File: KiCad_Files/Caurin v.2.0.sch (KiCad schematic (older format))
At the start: 23 parts, among them J1 ESQ-120-39-G-D, J2 Conn_01x12_Male, J3 Conn_01x09_Male, U1 STM32L476RGTx, Y1 32,768k

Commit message: Add shapes3D folder
Now all 3D models for the components are stored in a single folder, thanks to the Archive Plugin from https://github.com/MitjaNemec/Kicad_action_plugins.git
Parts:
- 16M1: symbol Device:Crystal_GND24 -> archive:Device_Crystal_GND24
- C1, C10, C2, C3, C4, C5, C6, C7, C8, C9: symbol Device:C_Small -> archive:Device_C_Small
- D1: symbol Device:LED -> archive:Device_LED
- J1: symbol SamacSys_Parts:ESQ-120-39-G-D -> archive:SamacSys_Parts_ESQ-120-39-G-D
- J2: symbol Connector:Conn_01x12_Male -> archive:Connector_Conn_01x12_Male
- J3: symbol Connector:Conn_01x09_Male -> archive:Connector_Conn_01x09_Male
- JP1: symbol Jumper:SolderJumper_3_Open -> archive:Jumper_SolderJumper_3_Open
- R1, R2, R3, R4: symbol Device:R_Small -> archive:Device_R_Small
- S1: symbol SamacSys_Parts:PTS636_SM43J_SMTR_LFS -> archive:SamacSys_Parts_PTS636_SM43J_SMTR_LFS
- U1: symbol MCU_ST_STM32L4:STM32L476RGTx -> archive:MCU_ST_STM32L4_STM32L476RGTx
- Y1: symbol Device:Crystal_Small -> archive:Device_Crystal_Small
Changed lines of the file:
@@
 	8550 5650 8600 5650
 $Comp
-L MCU_ST_STM32L4:STM32L476RGTx U1
+L archive:MCU_ST_STM32L4_STM32L476RGTx U1
 U 1 1 613E7615
 P 4625 5025
@@
 $EndComp
 $Comp
-L power:+3.3V #PWR0101
+L archive:power_+3.3V #PWR0101
 U 1 1 613F407B
 P 4675 3025
@@
 $EndComp
 $Comp
-L power:GND #PWR0102
+L archive:power_GND #PWR0102
 U 1 1 613FAFB6
 P 4625 6975
@@
 Connection ~ 4525 6925
 $Comp
-L Device:C_Small C2
+L archive:Device_C_Small C2
 U 1 1 614028ED
 P 4150 2050
@@
 $EndComp
 $Comp
-L Device:C_Small C7
+L archive:Device_C_Small C7
 U 1 1 6140503B
 P 4500 2050
@@
 $EndComp
 $Comp
-L Device:C_Small C8
+L archive:Device_C_Small C8
 U 1 1 614053AC
 P 4850 2050
@@
 $EndComp
 $Comp
-L Device:C_Small C9
+L archive:Device_C_Small C9
 U 1 1 6140585E
 P 5200 2050
@@
 $EndComp
 $Comp
-L Device:C_Small C1
+L archive:Device_C_Small C1
 U 1 1 61405AA7
 P 3800 2050
@@
 	4150 2250 4500 2250
 $Comp
-L power:+3.3V #PWR0103
+L archive:power_+3.3V #PWR0103
 U 1 1 61419BE2
 P 3800 1750
@@
 Connection ~ 3800 1850
 $Comp
-L power:GND #PWR0104
+L archive:power_GND #PWR0104
 U 1 1 6141BB41
 P 3800 2350
@@
 Connection ~ 3800 2250
 $Comp
-L Device:R_Small R2
+L archive:Device_R_Small R2
 U 1 1 6143BD59
 P 1900 3600
@@
 	2050 3600 2000 3600
 $Comp
-L Jumper:SolderJumper_3_Open JP1
+L archive:Jumper_SolderJumper_3_Open JP1
 U 1 1 61440C39
 P 1600 3600
@@
 	1750 3600 1800 3600
 $Comp
-L power:+3.3V #PWR0105
+L archive:power_+3.3V #PWR0105
 U 1 1 614479C3
 P 1600 3350
@@
 	1600 3350 1600 3400
 $Comp
-L power:GND #PWR0106
+L archive:power_GND #PWR0106
 U 1 1 61449D67
 P 1600 3850
@@
 	1600 3850 1600 3800
 $Comp
-L Device:Crystal_GND24 16M1
+L archive:Device_Crystal_GND24 16M1
 U 1 1 61450713
 P 1800 4950
@@
 $EndComp
 $Comp
-L power:GND #PWR0107
+L archive:power_GND #PWR0107
 U 1 1 61459354
 P 2725 5000
@@
 $EndComp
 $Comp
-L power:GND #PWR0108
+L archive:power_GND #PWR0108
 U 1 1 61459C79
 P 1325 5350
@@
 	2725 4950 2725 5000
 $Comp
-L Device:C_Small C3
+L archive:Device_C_Small C3
 U 1 1 6145E6A2
 P 1575 4700
@@
 	1800 4700 1800 4800
 $Comp
-L Device:C_Small C4
+L archive:Device_C_Small C4
 U 1 1 61463D13
 P 1575 5200
@@
 	3925 4725 3875 4725
 $Comp
-L power:GND #PWR0110
+L archive:power_GND #PWR0110
 U 1 1 614A349D
 P 1325 6650
@@
 	1325 6650 1325 6500
 $Comp
-L Device:C_Small C5
+L archive:Device_C_Small C5
 U 1 1 614A34A7
 P 1500 6125
@@
 	1400 6125 1325 6125
 $Comp
-L Device:C_Small C6
+L archive:Device_C_Small C6
 U 1 1 614A34B2
 P 1500 6500
@@
 	3925 6525 3875 6525
 $Comp
-L power:+3.3V #PWR0111
+L archive:power_+3.3V #PWR0111
 U 1 1 614C675D
 P 7350 2900
@@
 	7525 3125 7525 3075
 $Comp
-L power:GND #PWR0112
+L archive:power_GND #PWR0112
 U 1 1 614D5240
 P 7625 3125
@@
 	8425 3225 8425 3075
 $Comp
-L power:GND #PWR0113
+L archive:power_GND #PWR0113
 U 1 1 6158BF67
 P 1650 2600
@@
 $EndComp
 $Comp
-L Device:R_Small R1
+L archive:Device_R_Small R1
 U 1 1 6158C250
 P 1650 1750
@@
 $EndComp
 $Comp
-L power:+3.3V #PWR0114
+L archive:power_+3.3V #PWR0114
 U 1 1 6158C7F3
 P 1650 1550
@@
 	1650 1850 1650 1950
 $Comp
-L Device:C_Small C10
+L archive:Device_C_Small C10
 U 1 1 6159AFC7
 P 1850 2250
@@
 	3875 4925 3925 4925
 $Comp
-L Device:LED D1
+L archive:Device_LED D1
 U 1 1 61487691
 P 2700 2150
@@
 $EndComp
 $Comp
-L power:GND #PWR0109
+L archive:power_GND #PWR0109
 U 1 1 6149B9C4
 P 2700 2350
@@
 	2700 2300 2700 2350
 $Comp
-L Device:R_Small R4
+L archive:Device_R_Small R4
 U 1 1 614B0FAC
 P 2700 1850
@@
 	4675 3125 4725 3125
 $Comp
-L power:+3.3V #PWR0115
+L archive:power_+3.3V #PWR0115
 U 1 1 61613B7C
 P 7575 1250
@@
 GND
 $Comp
-L power:+5V #PWR0116
+L archive:power_+5V #PWR0116
 U 1 1 61683899
 P 6125 1850
@@
 $EndComp
 $Comp
-L power:+3.3V #PWR0117
+L archive:power_+3.3V #PWR0117
 U 1 1 61683C81
 P 6350 1850
@@
 $EndComp
 $Comp
-L power:GND #PWR0118
+L archive:power_GND #PWR0118
 U 1 1 61684B6A
 P 6250 2300
@@
 	8150 1450 8150 1275
 $Comp
-L power:+5V #PWR0119
+L archive:power_+5V #PWR0119
 U 1 1 61777ED3
 P 8775 1250
@@
 BUS_SCL1
 $Comp
-L Device:R_Small R3
+L archive:Device_R_Small R3
 U 1 1 614BCB98
 P 2050 5200
@@
 	7950 1450 7950 1275
 $Comp
-L power:GND #PWR0120
+L archive:power_GND #PWR0120
 U 1 1 6161F41F
 P 8050 1325
@@
 	1600 6500 1700 6500
 $Comp
-L Device:Crystal_Small Y1
+L archive:Device_Crystal_Small Y1
 U 1 1 614DD45F
 P 1700 6300
@@
 GND
 $Comp
-L SamacSys_Parts:ESQ-120-39-G-D J1
+L archive:SamacSys_Parts_ESQ-120-39-G-D J1
 U 1 1 613C51C6
 P 7650 6250
@@
 	10000 5950 10100 5950
 $Comp
-L SamacSys_Parts:PTS636_SM43J_SMTR_LFS S1
+L archive:SamacSys_Parts_PTS636_SM43J_SMTR_LFS S1
 U 1 1 6235C882
 P 1200 2250
@@
 Connection ~ 1650 2550
 $Comp
-L Connector:Conn_01x09_Male J3
+L archive:Connector_Conn_01x09_Male J3
 U 1 1 6251C245
 P 8250 1075
@@
 $EndComp
 $Comp
-L power:+BATT #PWR0152
+L archive:power_+BATT #PWR0152
 U 1 1 627D0227
 P 6625 1850
@@
 EXT_GPS_TX
 $Comp
-L Connector:Conn_01x12_Male J2
+L archive:Connector_Conn_01x12_Male J2
 U 1 1 6246EB1E
 P 8025 2875

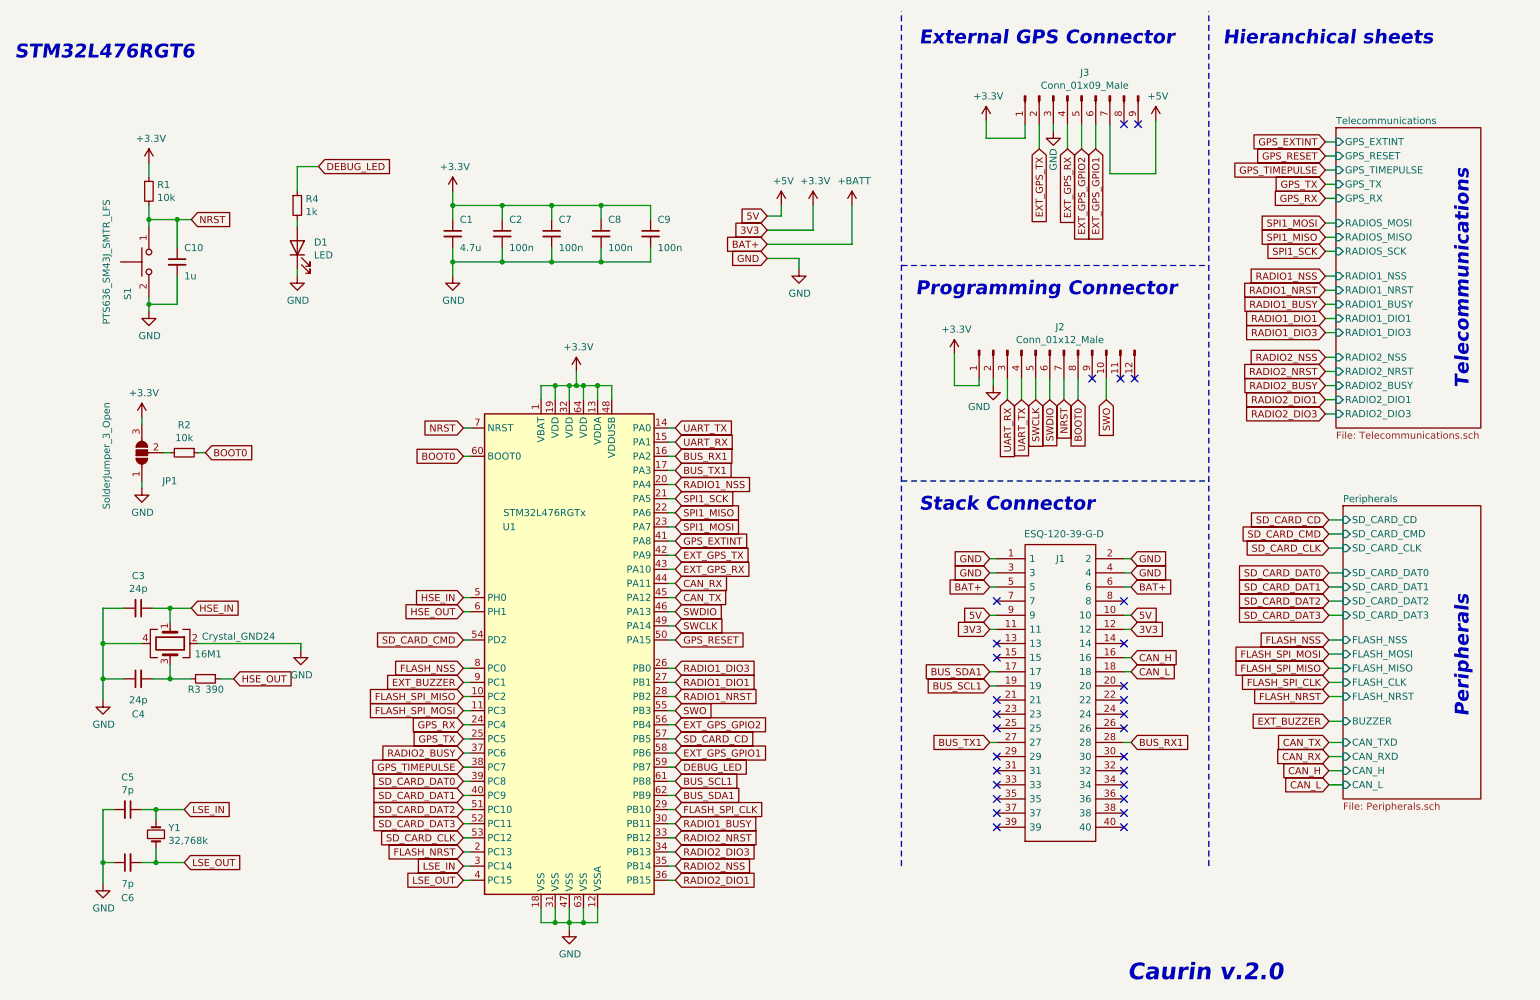
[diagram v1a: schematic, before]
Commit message: Add RTC backup battery
Add the CR1025 RTC Button Cell Battery. Update schematic images and PDF.
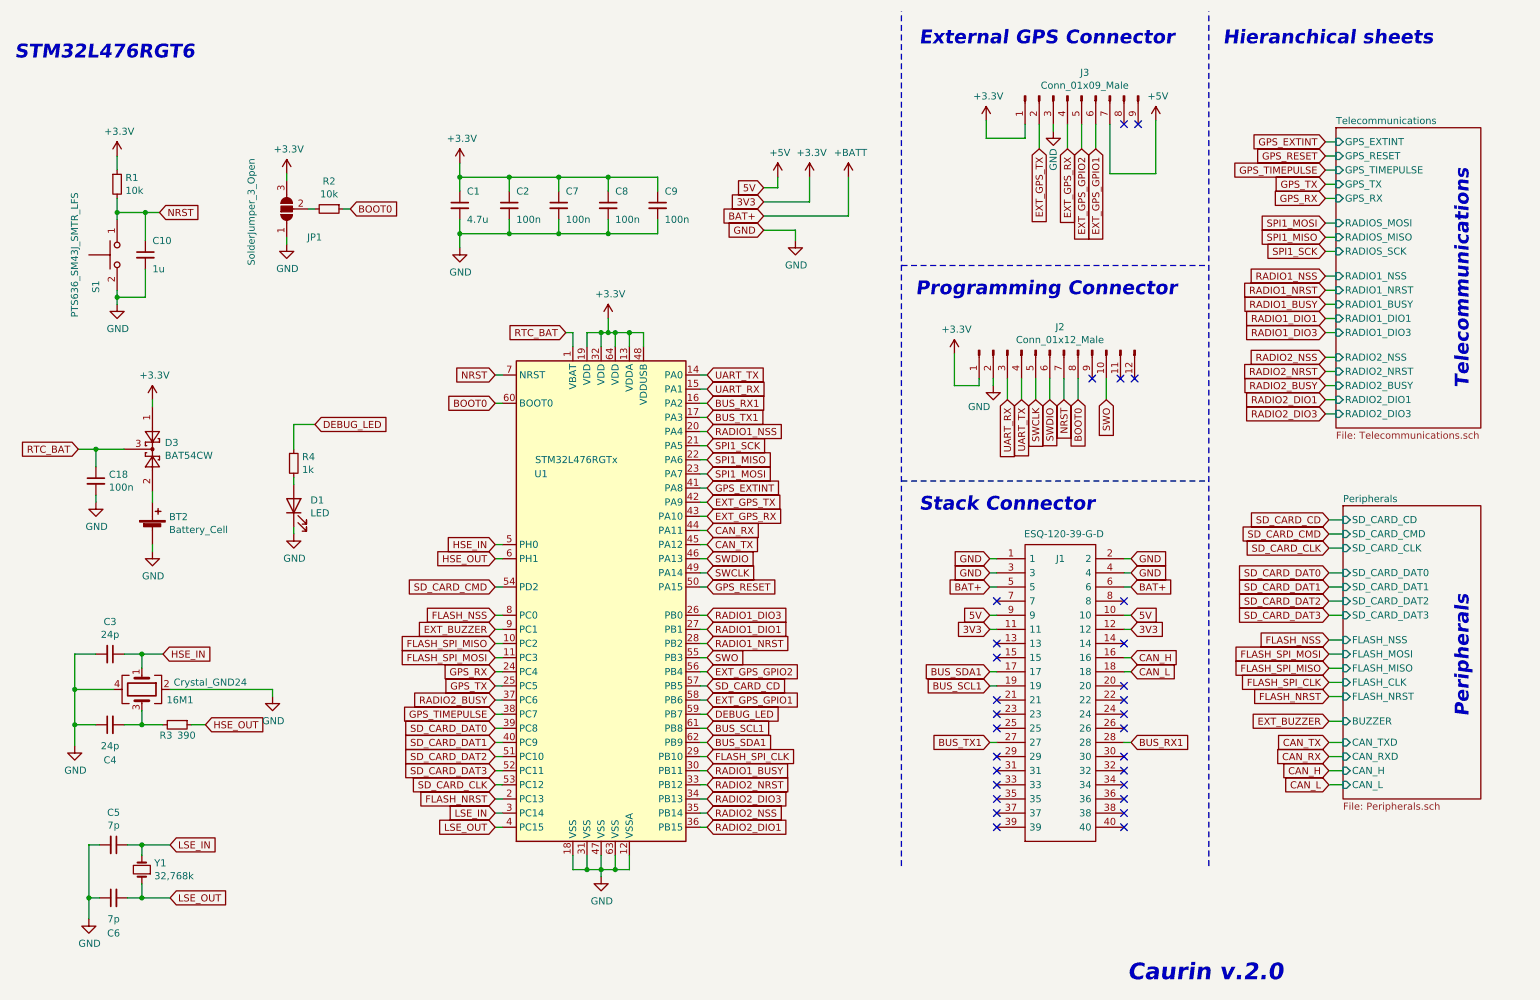
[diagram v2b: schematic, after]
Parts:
- added BT2: Battery_Cell, SamacSys_Parts:3030, symbol archive:Device_Battery_Cell
- added C18: 100n, Capacitor_SMD:C_0603_1608Metric, symbol archive:Device_C_Small
- added D3: BAT54CW, Package_TO_SOT_SMD:SOT-323_SC-70, symbol archive:Diode_BAT54CW
- C2, C7, C8, C9: footprint Capacitor_SMD:C_0805_2012Metric -> Capacitor_SMD:C_0603_1608Metric
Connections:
- net +3V3: now also D3.1; no longer U1.1 (VBAT)
- net GND: now also BT2.2 (-), C18.2
- new net: BT2.1 (+), D3.2
- new net RTC_BAT: C18.1, D3.3, U1.1 (VBAT)
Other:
- moved on the sheet: 16M1, C1, C10, C2, C3, C4, C5, C6, C7, C8, C9, D1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
